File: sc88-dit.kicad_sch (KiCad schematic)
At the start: 56 parts, among them J1 Conn_01x04_Male, J2 Conn_01x04_Male, J3 Conn_01x06_Male, J4 Conn_01x06_Male, U1 74LVC1G74, U2 AK4103A

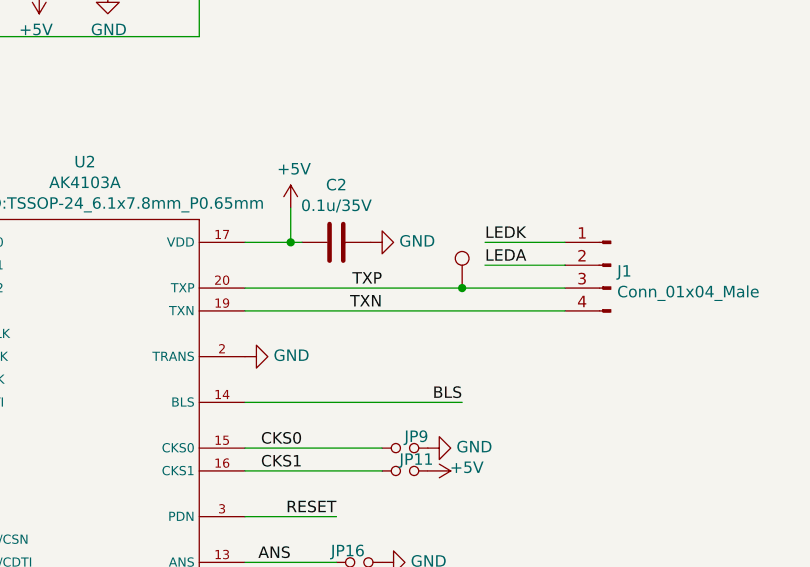
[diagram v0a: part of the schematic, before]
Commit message: Added TXP/TXN jumper(or resistor)
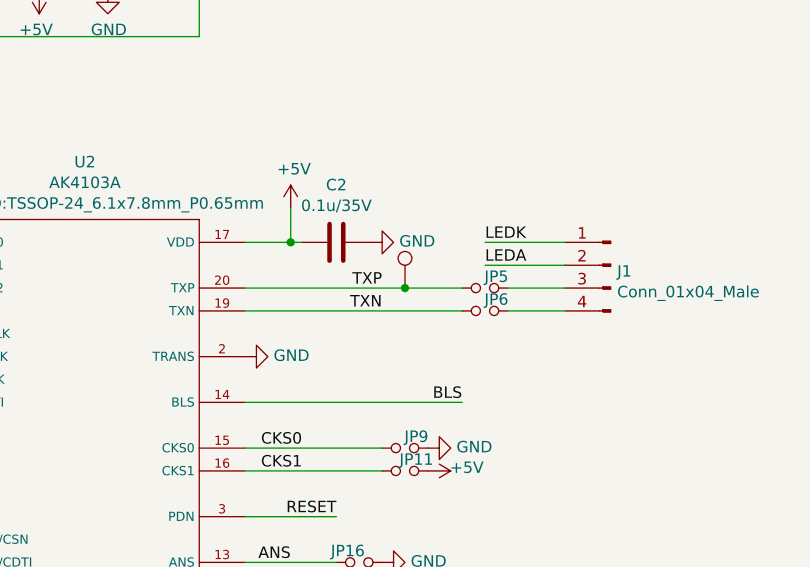
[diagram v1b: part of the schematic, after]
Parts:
- added JP5, JP6: Jumper_NO_Small, components:R_0603_1608Metric_SolderJumperCompatible, symbol Device:Jumper_NO_Small
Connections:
- net TXN: now also JP6.2; no longer J1.4 (Pin_4)
- net TXP: now also JP5.2; no longer J1.3 (Pin_3)
- new net: J1.3 (Pin_3), JP5.1
- new net: J1.4 (Pin_4), JP6.1
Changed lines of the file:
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@@
   (junction (at 173.99 95.25) (diameter 0) (color 0 0 0 0))
   (junction (at 176.53 46.99) (diameter 0) (color 0 0 0 0))
-  (junction (at 193.04 100.33) (diameter 0) (color 0 0 0 0))
+  (junction (at 186.69 100.33) (diameter 0) (color 0 0 0 0))
   (wire (pts (xy 29.21 83.82) (xy 41.91 83.82))
     (stroke (width 0) (type solid) (color 0 0 0 0))
@@
     (stroke (width 0) (type solid) (color 0 0 0 0))
   )
-  (wire (pts (xy 168.91 100.33) (xy 193.04 100.33))
-    (stroke (width 0) (type solid) (color 0 0 0 0))
-  )
-  (wire (pts (xy 168.91 102.87) (xy 204.47 102.87))
+  (wire (pts (xy 168.91 100.33) (xy 186.69 100.33))
+    (stroke (width 0) (type solid) (color 0 0 0 0))
+  )
+  (wire (pts (xy 168.91 102.87) (xy 193.04 102.87))
     (stroke (width 0) (type solid) (color 0 0 0 0))
   )
@@
     (stroke (width 0) (type solid) (color 0 0 0 0))
   )
-  (wire (pts (xy 193.04 100.33) (xy 204.47 100.33))
+  (wire (pts (xy 186.69 100.33) (xy 193.04 100.33))
     (stroke (width 0) (type solid) (color 0 0 0 0))
   )
@@
   )
   (wire (pts (xy 195.58 97.79) (xy 204.47 97.79))
+    (stroke (width 0) (type solid) (color 0 0 0 0))
+  )
+  (wire (pts (xy 198.12 100.33) (xy 204.47 100.33))
+    (stroke (width 0) (type solid) (color 0 0 0 0))
+  )
+  (wire (pts (xy 198.12 102.87) (xy 204.47 102.87))
     (stroke (width 0) (type solid) (color 0 0 0 0))
   )
@@
     )
   )
+  (symbol (lib_id "Device:Jumper_NO_Small") (at 195.58 100.33 0) (mirror y) (unit 1)
+    (in_bom yes) (on_board yes)
+    (property "Reference" "JP5" (id 0) (at 196.85 99.06 0))
+    (property "Value" "Jumper_NO_Small" (id 1) (at 195.58 98.037 0)
+      (effects (font (size 1.27 1.27)) hide)
+    )
+    (property "Footprint" "components:R_0603_1608Metric_SolderJumperCompatible" (id 2) (at 195.58 100.33 0)
+      (effects (font (size 1.27 1.27)) hide)
+    )
+    (property "Datasheet" "~" (id 3) (at 195.58 100.33 0)
+      (effects (font (size 1.27 1.27)) hide)
+    )
+  )
+  (symbol (lib_id "Device:Jumper_NO_Small") (at 195.58 102.87 0) (mirror y) (unit 1)
+    (in_bom yes) (on_board yes)
+    (property "Reference" "JP6" (id 0) (at 196.85 101.6 0))
+    (property "Value" "Jumper_NO_Small" (id 1) (at 195.58 100.577 0)
+      (effects (font (size 1.27 1.27)) hide)
+    )
+    (property "Footprint" "components:R_0603_1608Metric_SolderJumperCompatible" (id 2) (at 195.58 102.87 0)
+      (effects (font (size 1.27 1.27)) hide)
+    )
+    (property "Datasheet" "~" (id 3) (at 195.58 102.87 0)
+      (effects (font (size 1.27 1.27)) hide)
+    )
+  )
   (symbol (lib_id "Connector:TestPoint") (at 62.23 88.9 90) (unit 1)
     (in_bom yes) (on_board yes)
@@
     )
   )
+  (symbol (lib_id "Connector:TestPoint") (at 186.69 100.33 0) (unit 1)
+    (in_bom yes) (on_board yes)
+    (property "Reference" "TP4" (id 0) (at 185.541 95.631 90)
+      (effects (font (size 1.27 1.27)) (justify left) hide)
+    )
+    (property "Value" "TestPoint" (id 1) (at 187.839 95.631 90)
+      (effects (font (size 1.27 1.27)) (justify left) hide)
+    )
+    (property "Footprint" "Connector_PinHeader_2.54mm:PinHeader_1x01_P2.54mm_Vertical" (id 2) (at 191.77 100.33 0)
+      (effects (font (size 1.27 1.27)) hide)
+    )
+    (property "Datasheet" "~" (id 3) (at 191.77 100.33 0)
+      (effects (font (size 1.27 1.27)) hide)
+    )
+  )
   (symbol (lib_id "Connector:TestPoint") (at 193.04 46.99 270) (unit 1)
     (in_bom yes) (on_board yes)
@@
     )
     (property "Datasheet" "~" (id 3) (at 193.04 52.07 0)
-      (effects (font (size 1.27 1.27)) hide)
-    )
-  )
-  (symbol (lib_id "Connector:TestPoint") (at 193.04 100.33 0) (unit 1)
-    (in_bom yes) (on_board yes)
-    (property "Reference" "TP4" (id 0) (at 191.891 95.631 90)
-      (effects (font (size 1.27 1.27)) (justify left) hide)
-    )
-    (property "Value" "TestPoint" (id 1) (at 194.189 95.631 90)
-      (effects (font (size 1.27 1.27)) (justify left) hide)
-    )
-    (property "Footprint" "Connector_PinHeader_2.54mm:PinHeader_1x01_P2.54mm_Vertical" (id 2) (at 198.12 100.33 0)
-      (effects (font (size 1.27 1.27)) hide)
-    )
-    (property "Datasheet" "~" (id 3) (at 198.12 100.33 0)
       (effects (font (size 1.27 1.27)) hide)
     )
@@
   (symbol (lib_id "power:GND") (at 168.91 107.95 90) (unit 1)
     (in_bom yes) (on_board yes)
-    (property "Reference" "#PWR?" (id 0) (at 175.26 107.95 0)
+    (property "Reference" "#PWR0112" (id 0) (at 175.26 107.95 0)
       (effects (font (size 1.27 1.27)) hide)
     )
@@
       (reference "#PWR0111") (unit 1)
     )
+    (path "/286a2fe5-fa63-401e-8b5b-12f1d7182d49"
+      (reference "#PWR0112") (unit 1)
+    )
     (path "/a341d8f1-0f9a-4f15-a44d-69ed966b1ad6"
       (reference "#PWR0116") (unit 1)
@@
       (reference "#PWR0128") (unit 1)
     )
-    (path "/286a2fe5-fa63-401e-8b5b-12f1d7182d49"
-      (reference "#PWR?") (unit 1)
-    )
     (path "/19bc91f9-0a5c-4169-879c-06fb2311b989"
       (reference "C1") (unit 1)
@@
       (reference "JP4") (unit 1)
     )
+    (path "/875bec72-ffc1-42dc-9942-2ff54e597dcd"
+      (reference "JP5") (unit 1)
+    )
+    (path "/94b93a8c-ba6a-4617-b300-c1e857b731f5"
+      (reference "JP6") (unit 1)
+    )
     (path "/73d2abff-24c2-48df-8693-6c9fd9b96183"

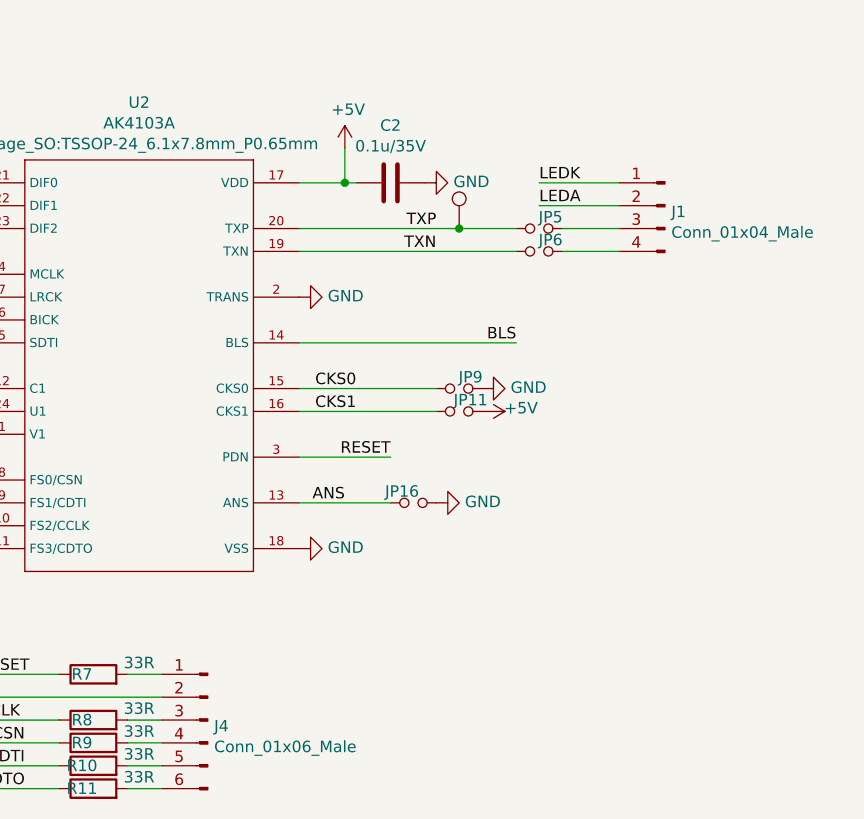
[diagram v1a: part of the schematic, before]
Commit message: To use right-angle connectors
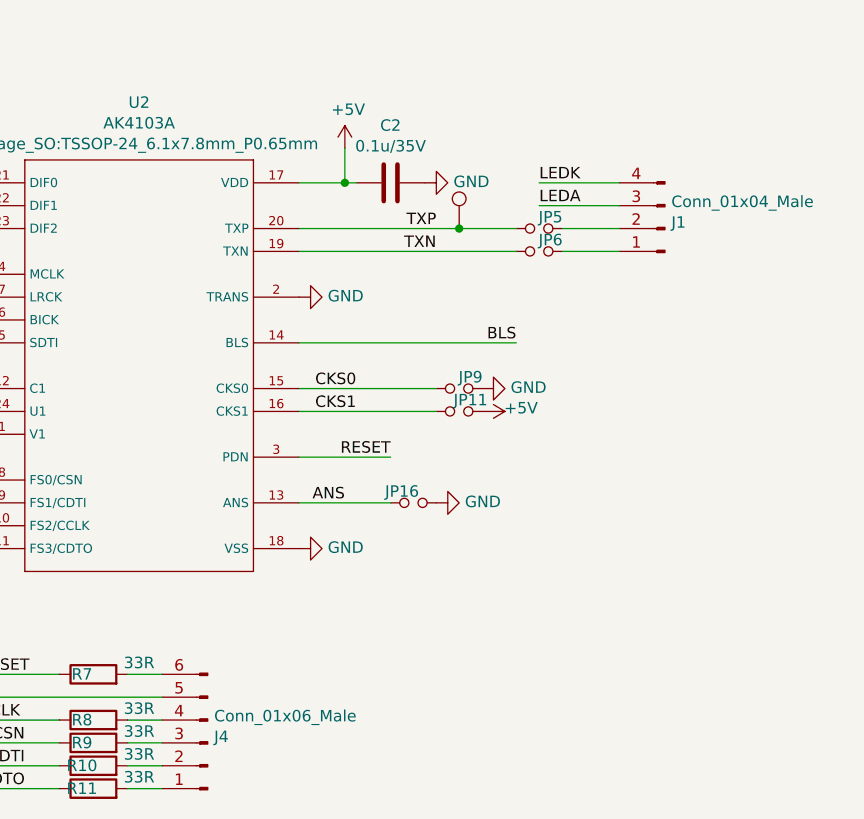
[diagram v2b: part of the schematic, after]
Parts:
- J1, J2: footprint Connector_JST:JST_XH_B4B-XH-A_1x04_P2.50mm_Vertical -> Connector_JST:JST_XH_S4B-XH-A-1_1x04_P2.50mm_Horizontal
- J3, J4: footprint Connector_JST:JST_XH_B6B-XH-A_1x06_P2.50mm_Vertical -> Connector_JST:JST_XH_S6B-XH-A-1_1x06_P2.50mm_Horizontal
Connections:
- net GND: now also J4.5 (Pin_5); no longer J4.2 (Pin_2)
- net LEDA: now also J1.3 (Pin_3); no longer J1.2 (Pin_2)
- net LEDK: now also J1.4 (Pin_4); no longer J1.1 (Pin_1)
- net at J4.1 (Pin_1): now also R11.2; no longer R7.2
- net at J4.3 (Pin_3): now also R9.2; no longer R8.2
- net at J4.4 (Pin_4): now also R8.2; no longer R9.2
- net at R10.2: now also J4.2 (Pin_2); no longer J4.5 (Pin_5)
- net at J4.6 (Pin_6): now also R7.2; no longer R11.2
- net at JP5.1: now also J1.2 (Pin_2); no longer J1.3 (Pin_3)
- net at JP6.1: now also J1.1 (Pin_1); no longer J1.4 (Pin_4)
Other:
- moved on the sheet: J1, J4
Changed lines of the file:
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@@
     (property "Reference" "J2" (id 0) (at 26.8224 79.3558 0))
     (property "Value" "Conn_01x04_Male" (id 1) (at 26.8224 81.6545 0))
-    (property "Footprint" "Connector_JST:JST_XH_B4B-XH-A_1x04_P2.50mm_Vertical" (id 2) (at 24.13 86.36 0)
+    (property "Footprint" "Connector_JST:JST_XH_S4B-XH-A-1_1x04_P2.50mm_Horizontal" (id 2) (at 24.13 86.36 0)
       (effects (font (size 1.27 1.27)) hide)
     )
@@
     )
   )
-  (symbol (lib_id "Connector:Conn_01x04_Male") (at 209.55 97.79 0) (mirror y) (unit 1)
+  (symbol (lib_id "Connector:Conn_01x04_Male") (at 209.55 100.33 180) (unit 1)
     (in_bom yes) (on_board yes)
-    (property "Reference" "J1" (id 0) (at 210.2613 98.4694 0)
+    (property "Reference" "J1" (id 0) (at 210.2613 99.6506 0)
       (effects (font (size 1.27 1.27)) (justify right))
     )
-    (property "Value" "Conn_01x04_Male" (id 1) (at 210.2613 100.7681 0)
+    (property "Value" "Conn_01x04_Male" (id 1) (at 210.2613 97.3519 0)
       (effects (font (size 1.27 1.27)) (justify right))
     )
-    (property "Footprint" "Connector_JST:JST_XH_B4B-XH-A_1x04_P2.50mm_Vertical" (id 2) (at 209.55 97.79 0)
+    (property "Footprint" "Connector_JST:JST_XH_S4B-XH-A-1_1x04_P2.50mm_Horizontal" (id 2) (at 209.55 100.33 0)
       (effects (font (size 1.27 1.27)) hide)
     )
-    (property "Datasheet" "~" (id 3) (at 209.55 97.79 0)
+    (property "Datasheet" "~" (id 3) (at 209.55 100.33 0)
       (effects (font (size 1.27 1.27)) hide)
     )
@@
     (property "Reference" "J3" (id 0) (at 26.8224 95.8658 0))
     (property "Value" "Conn_01x06_Male" (id 1) (at 26.8224 98.1645 0))
-    (property "Footprint" "Connector_JST:JST_XH_B6B-XH-A_1x06_P2.50mm_Vertical" (id 2) (at 24.13 105.41 0)
+    (property "Footprint" "Connector_JST:JST_XH_S6B-XH-A-1_1x06_P2.50mm_Horizontal" (id 2) (at 24.13 105.41 0)
       (effects (font (size 1.27 1.27)) hide)
     )
@@
     )
   )
-  (symbol (lib_id "Connector:Conn_01x06_Male") (at 158.75 154.94 0) (mirror y) (unit 1)
+  (symbol (lib_id "Connector:Conn_01x06_Male") (at 158.75 157.48 180) (unit 1)
     (in_bom yes) (on_board yes)
-    (property "Reference" "J4" (id 0) (at 159.4613 155.6194 0)
+    (property "Reference" "J4" (id 0) (at 159.4613 156.8006 0)
       (effects (font (size 1.27 1.27)) (justify right))
     )
-    (property "Value" "Conn_01x06_Male" (id 1) (at 159.4613 157.9181 0)
+    (property "Value" "Conn_01x06_Male" (id 1) (at 159.4613 154.5019 0)
       (effects (font (size 1.27 1.27)) (justify right))
     )
-    (property "Footprint" "Connector_JST:JST_XH_B6B-XH-A_1x06_P2.50mm_Vertical" (id 2) (at 158.75 154.94 0)
+    (property "Footprint" "Connector_JST:JST_XH_S6B-XH-A-1_1x06_P2.50mm_Horizontal" (id 2) (at 158.75 157.48 0)
       (effects (font (size 1.27 1.27)) hide)
     )
-    (property "Datasheet" "~" (id 3) (at 158.75 154.94 0)
+    (property "Datasheet" "~" (id 3) (at 158.75 157.48 0)
       (effects (font (size 1.27 1.27)) hide)
     )

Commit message: Added NB3N511 clock multiplier to make MCLK from BCLK
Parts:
- added C11: 0.1u/35V, Capacitor_SMD:C_0603_1608Metric_Pad1.05x0.95mm_HandSolder, symbol Device:C
- added JP10, JP12, JP7, JP8: Jumper_NO_Small, components:R_0603_1608Metric_SolderJumperCompatible, symbol Device:Jumper_NO_Small
- added U3: NB3N511, Package_SO:SOIC-8_3.9x4.9mm_P1.27mm, symbol Oscillator:NB3N511
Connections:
- net +5V: now also C11.1, JP10.1, JP7.1, U3.2 (VDD)
- net GND: now also C11.2, JP12.2, JP8.2, U3.3 (GND)
- net MULDIV_CLK: now reaches R1.1, U1.5 (Q)
- net MULDIV_CLK: now also U3.5 (CLKOUT)
- net BLK renamed BICK
- net BICK: now also U3.1 (X1/ICLK)
- new net I511_S0: JP7.2, JP8.1, U3.6 (S0)
- new net I511_S1: JP10.2, JP12.1, U3.4 (S1)
- no-connect marks 0 -> 2

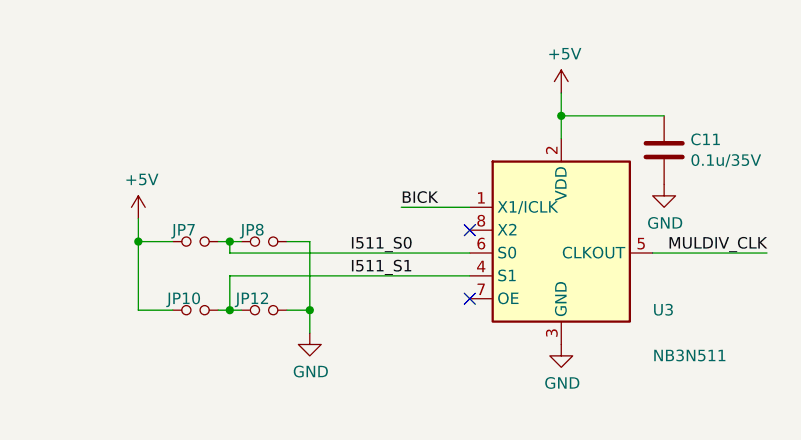
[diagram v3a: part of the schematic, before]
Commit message: To be able to select multiplier's input from MCLK and BICK
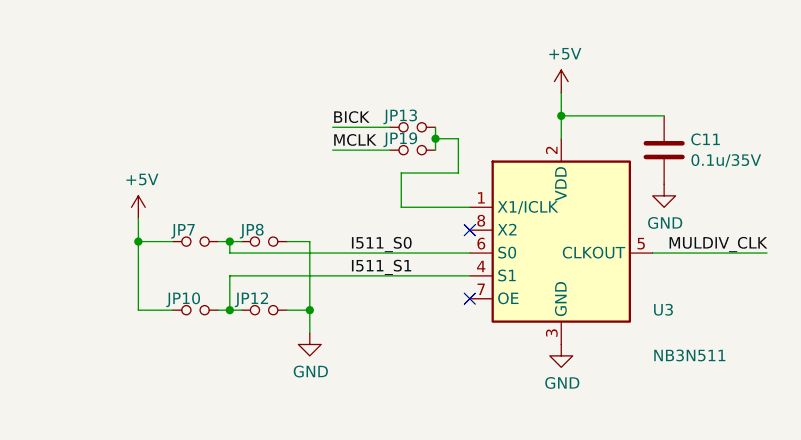
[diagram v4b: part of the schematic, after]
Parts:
- added JP13, JP19: Jumper_NO_Small, components:R_0603_1608Metric_SolderJumperCompatible, symbol Device:Jumper_NO_Small
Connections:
- net BICK: now also JP13.1; no longer U3.1 (X1/ICLK)
- net MCLK: now also JP19.1
- new net: JP13.2, JP19.2, U3.1 (X1/ICLK)
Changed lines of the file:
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@@
   (junction (at 54.61 110.49) (diameter 0) (color 0 0 0 0))
   (junction (at 57.15 113.03) (diameter 0) (color 0 0 0 0))
+  (junction (at 63.5 34.29) (diameter 0) (color 0 0 0 0))
   (junction (at 63.5 102.87) (diameter 0) (color 0 0 0 0))
   (junction (at 68.58 105.41) (diameter 0) (color 0 0 0 0))
@@
     (stroke (width 0) (type solid) (color 0 0 0 0))
   )
+  (wire (pts (xy 52.07 33.02) (xy 58.42 33.02))
+    (stroke (width 0) (type solid) (color 0 0 0 0))
+  )
+  (wire (pts (xy 52.07 35.56) (xy 58.42 35.56))
+    (stroke (width 0) (type solid) (color 0 0 0 0))
+  )
   (wire (pts (xy 54.61 110.49) (xy 36.83 110.49))
     (stroke (width 0) (type solid) (color 0 0 0 0))
@@
     (stroke (width 0) (type solid) (color 0 0 0 0))
   )
+  (wire (pts (xy 59.69 38.1) (xy 66.04 38.1))
+    (stroke (width 0) (type solid) (color 0 0 0 0))
+  )
+  (wire (pts (xy 59.69 41.91) (xy 59.69 38.1))
+    (stroke (width 0) (type solid) (color 0 0 0 0))
+  )
   (wire (pts (xy 59.69 41.91) (xy 67.31 41.91))
     (stroke (width 0) (type solid) (color 0 0 0 0))
   )
+  (wire (pts (xy 63.5 33.02) (xy 63.5 34.29))
+    (stroke (width 0) (type solid) (color 0 0 0 0))
+  )
+  (wire (pts (xy 63.5 34.29) (xy 63.5 35.56))
+    (stroke (width 0) (type solid) (color 0 0 0 0))
+  )
   (wire (pts (xy 63.5 102.87) (xy 96.52 102.87))
     (stroke (width 0) (type solid) (color 0 0 0 0))
@@
     (stroke (width 0) (type solid) (color 0 0 0 0))
   )
+  (wire (pts (xy 66.04 34.29) (xy 63.5 34.29))
+    (stroke (width 0) (type solid) (color 0 0 0 0))
+  )
+  (wire (pts (xy 66.04 38.1) (xy 66.04 34.29))
+    (stroke (width 0) (type solid) (color 0 0 0 0))
+  )
   (wire (pts (xy 67.31 46.99) (xy 40.64 46.99))
     (stroke (width 0) (type solid) (color 0 0 0 0))
@@
     (effects (font (size 1.27 1.27)) (justify right bottom))
   )
-  (label "BICK" (at 59.69 41.91 0)
+  (label "BICK" (at 52.07 33.02 0)
+    (effects (font (size 1.27 1.27)) (justify left bottom))
+  )
+  (label "MCLK" (at 52.07 35.56 0)
     (effects (font (size 1.27 1.27)) (justify left bottom))
   )
@@
     )
     (property "Datasheet" "~" (id 3) (at 44.45 53.34 0)
+      (effects (font (size 1.27 1.27)) hide)
+    )
+  )
+  (symbol (lib_id "Device:Jumper_NO_Small") (at 60.96 33.02 0) (unit 1)
+    (in_bom yes) (on_board yes)
+    (property "Reference" "JP13" (id 0) (at 59.69 31.75 0))
+    (property "Value" "Jumper_NO_Small" (id 1) (at 60.96 30.727 0)
+      (effects (font (size 1.27 1.27)) hide)
+    )
+    (property "Footprint" "components:R_0603_1608Metric_SolderJumperCompatible" (id 2) (at 60.96 33.02 0)
+      (effects (font (size 1.27 1.27)) hide)
+    )
+    (property "Datasheet" "~" (id 3) (at 60.96 33.02 0)
+      (effects (font (size 1.27 1.27)) hide)
+    )
+  )
+  (symbol (lib_id "Device:Jumper_NO_Small") (at 60.96 35.56 0) (unit 1)
+    (in_bom yes) (on_board yes)
+    (property "Reference" "JP19" (id 0) (at 59.69 34.29 0))
+    (property "Value" "Jumper_NO_Small" (id 1) (at 60.96 33.267 0)
+      (effects (font (size 1.27 1.27)) hide)
+    )
+    (property "Footprint" "components:R_0603_1608Metric_SolderJumperCompatible" (id 2) (at 60.96 35.56 0)
+      (effects (font (size 1.27 1.27)) hide)
+    )
+    (property "Datasheet" "~" (id 3) (at 60.96 35.56 0)
       (effects (font (size 1.27 1.27)) hide)
     )
@@
       (reference "JP12") (unit 1)
     )
+    (path "/d6730af0-ebc0-491a-95d6-f162c0fb6b19"
+      (reference "JP13") (unit 1)
+    )
     (path "/416e406e-2b88-41d5-b8f5-4091c71d70e5"
       (reference "JP14") (unit 1)
@@
       (reference "JP18") (unit 1)
     )
+    (path "/7f48657d-3ffd-4a0d-b548-81cf4f5eeeac"
+      (reference "JP19") (unit 1)
+    )
     (path "/d9a113dc-2e9c-449c-a11c-6f206fe5c040"
